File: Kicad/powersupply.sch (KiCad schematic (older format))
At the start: 1 part, among them J601 USB_B

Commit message: Completed PSU design.
Also changed footprint for stacked USB connector to change
shield pins from SHx to Pin 9.
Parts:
- removed J601: USB_B, Connector_USB:USB_B_OST_USB-B1HSxx_Horizontal, symbol Connector:USB_B
- added C601, C602: 100u, Capacitor_THT:CP_Radial_D6.3mm_P2.50mm, symbol Device:CP
- added C603: 22u, Capacitor_THT:CP_Radial_D6.3mm_P2.50mm, symbol Device:CP
- added C604, C608: 100n, Capacitor_SMD:C_0805_2012Metric_Pad1.15x1.40mm_HandSolder, symbol Device:C
- added C605: 47u, Capacitor_THT:CP_Radial_D6.3mm_P2.50mm, symbol Device:CP
- added C606: 1u, Capacitor_THT:CP_Radial_D6.3mm_P2.50mm, symbol Device:CP
- added C607: 4u7, Capacitor_THT:CP_Radial_D6.3mm_P2.50mm, symbol Device:CP
- added D601: LED, LED_THT:LED_D3.0mm, symbol Device:LED
- added F601: 5A Polyfuse, Fuse:Fuse_Littelfuse_395Series, symbol Device:Polyfuse
- added J601: Jack-DC, Connector_BarrelJack:BarrelJack_CUI_PJ-063AH_Horizontal, symbol Connector:Jack-DC
- added J602: Conn_01x04, Connector_PinSocket_2.54mm:PinSocket_1x04_P2.54mm_Vertical, symbol Connector_Generic:Conn_01x04
- added J603: Double-mini-DIN-6, Neotron-Common-Hardware:Double_mini-DIN_6, symbol Neotron-Common-Hardware:Double-mini-DIN-6
- added L601: 22u, Inductor_THT:L_Axial_L23.4mm_D12.7mm_P7.62mm_Vertical_Vishay_IHA-203, symbol Device:L
- added R601, R602, R603, R604, R605, R606: 100k, Resistor_SMD:R_0805_2012Metric_Pad1.15x1.40mm_HandSolder, symbol Device:R
- added R607: 1k, Resistor_SMD:R_0805_2012Metric_Pad1.15x1.40mm_HandSolder, symbol Device:R
- added RN601: 2k7 x 4, Resistor_THT:R_Array_SIP5, symbol Device:R_Network04
- added SW601, SW602: SW_DIP_x01, Connector_PinHeader_2.54mm:PinHeader_1x02_P2.54mm_Vertical, symbol Switch:SW_DIP_x01
- added TP601: TestPoint, TestPoint:TestPoint_THTPad_2.0x2.0mm_Drill1.0mm, symbol Connector:TestPoint
- added U601: K7805-3AR3, Connector_PinSocket_2.54mm:PinSocket_1x12_P2.54mm_Vertical, symbol Neotron-Common-Hardware:K78xx-3AR3
- added U602: AMS1117CD-3.3, Package_TO_SOT_SMD:TO-252-3_TabPin2, symbol Regulator_Linear:AMS1117CD-3.3
- added U603: MAX1615xUK, Package_TO_SOT_SMD:SOT-23-5, symbol Regulator_Linear:MAX1615xUK
- added U604: NUC029FAE, Package_SO:TSSOP-20_4.4x6.5mm_P0.65mm, symbol Neotron-Common-Hardware:NUC029FAE
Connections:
- net labels added: +3.3V, +3V3, +5V, +5VP, DC_ON, GND, I2C_SCL, I2C_SDA, ICE_CLK, ICE_DAT, IRQ, MONITOR_3V3, MONITOR_5V, PS2_CLK0, PS2_CLK1, PS2_DAT0, PS2_DAT1, STATUS_LED, UART0_TX, ~POWER_SW, ~RESET, ~RESET_OUT, ~RESET_SW
- wire segments 0 -> 140
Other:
- note added: "2.51mm (inner, 5.5mm outer diameter) barrel\njack. Centre +ve. 8V to 28V input."
- note added: "28V max input\n30mA max output"
- note added: "36V max input\n3A max output"
- note added: "BSP Debug"
- note added: "Board Management MCU"
- note added: "Dual mini-DIN 6 connectors for PS/2 Keyboard and PS/2 Mouse.\nSignalling is 5V open-collector, with pull-up required.\n\nKeyboard max current is 275 mA so cannot be run from\nstandby regulator."
- note added: "Keyboard"
- note added: "Main Power Regulators"
- note added: "Manual reset switch"
- note added: "Most of our board runs on 3.3V. We expect\nto draw around 100 mA from this 1A linear\nregulator.\n\nMax power wasted: (5V - 3.3V) * 1A = 1.7W\n\nAt 50 °C/W that's 85 °C over ambient at the\njunction - so use a heatsink if you want to\npull over 250 mA. Or replace with a\n3-terminal switching PSU module."
- note added: "Mouse"
- note added: "PS/2 Keyboard and Mouse Interface"
- note added: "Place near U604"
- note added: "Soft power switch"
- note added: "Some of our board (e.g. USB) runs on 5V. We need to\nsupply 2A (4x500mA) to downstream USB devices.\nWe use a big 3A/5V DC-DC to supply this."
- note added: "This MCU controls power/reset.\n\nLines to host are tri-state until host is\npowered to avoid back-powering."
- note added: "This small PSU runs our\nboard management MCU"
- note removed: "The USB Type-B port is used as a 5V input for the system.\nYou could use a 2.51mm (inner, 5.5mm outer diameter) barrel\njack instead."

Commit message: Replaced NUC029 (TSSOP) with KE04 (SOIC).
Also updated the BOM with some part nos.
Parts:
- removed U604: NUC029FAE, Package_SO:TSSOP-20_4.4x6.5mm_P0.65mm, symbol Neotron-Common-Hardware:NUC029FAE
- added R605: 33k, Resistor_SMD:R_0805_2012Metric_Pad1.15x1.40mm_HandSolder, symbol Device:R
- added U604: MKE04P24M48SF0, Package_SO:SOIC-20W_7.5x12.8mm_P1.27mm, symbol Neotron-Common-Hardware:MKE04P24M48SF0
- C601, C602: value 100u -> 100u 50V; DNP (none) -> 0
- C603, C605, C607, D601, J602, L601, R601, R602, R603, RN601, SW601, SW602: DNP (none) -> 0
- C604, C608: DNP (none) -> 0; Digikey (none) -> BC1150CT-ND; MPN (none) -> K104K15X7RF5TL2; Manufacturer (none) -> Vishay
- C606: value 1u -> 1u 50V; DNP (none) -> 0; Digikey (none) -> 493-10944-1-ND; MPN (none) -> UFG1H010MDM1TD; Manufacturer (none) -> Nichicon
- F601: value 5A Polyfuse -> 6A PTC; footprint Fuse:Fuse_Littelfuse_395Series -> Fuse:Fuse_Bourns_MF-RG500; DNP (none) -> 0; Digikey (none) -> MF-R500-2CT-ND; MPN (none) -> MF-R500-2; Manufacturer (none) -> Bourns
- J601: DNP (none) -> 0; Digikey (none) -> CP-063AH-ND; MPN (none) -> PJ-063AH; Manufacturer (none) -> CUI
- J603: MPN (none) -> KMDGX-6S/6S-S4N; Manufacturer (none) -> Kycon
- R604: value 100k -> 1k; DNP (none) -> 0
- R606: renamed from R605; DNP (none) -> 0
- R607: value 1k -> 100k; DNP (none) -> 0
- R608: renamed from R606; DNP (none) -> 0
- TP601: value TestPoint -> Reset; DNP (none) -> 0
- U601: value K7805-3AR3 -> 5V DC-DC Module; DNP (none) -> 0; Digikey (none) -> 2725-K7805-3AR3-ND; MPN (none) -> K7805-3AR3; Manufacturer Mornsun -> Mornsun America, LLC
- U602: value AMS1117CD-3.3 -> 3v3 LDO; DNP (none) -> 0; Digikey (none) -> ZLDO1117K33DICT-ND; MPN (none) -> ZLDO1117K33TC; Manufacturer (none) -> Diodes Incorporated
- U603: value MAX1615xUK -> MAX1615; DNP (none) -> 0; Digikey (none) -> MAX1615EUK+TCT-ND; MPN (none) -> MAX1615; Manufacturer (none) -> Maxim
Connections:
- net labels added: MON_3V3, MON_5V, SWDCLK, SWDIO
- net labels removed: ICE_CLK, ICE_DAT, MONITOR_3V3, MONITOR_5V, ~RESET_OUT
- wire segments 140 -> 144
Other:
- note added: "BMC Debug"
- note added: "Board Management Controller"
- note added: "Manual reset switch:\nTap for reset"
- note added: "Soft power switch:\nTap for On/Shutdown\nHold for Off"
- note added: "The BMC controls power/reset, as well\nas PS/2 devices and performing voltage\nrail monitoring.\n\nLines to host are hi-Z until host is\npowered (i.e. 3.3V looks good) to\navoid back-powering."
- note removed: "BSP Debug"
- note removed: "Board Management MCU"
- note removed: "Manual reset switch"
- note removed: "Soft power switch"
- note removed: "This MCU controls power/reset.\n\nLines to host are tri-state until host is\npowered to avoid back-powering."
- moved on the sheet: C608, R606, R608, SW601, SW602, TP601

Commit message: Make CPU card bigger.
Just big enough to take a TQFP-176 now.
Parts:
- TP601: DNP 0 -> 1
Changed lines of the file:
@@
 $Descr A4 11693 8268
 encoding utf-8
-Sheet 6 9
+Sheet 6 8
 Title "Neotron Common Hardware - Power Supply"
 Date "2020-12-26"
@@
 F 2 "TestPoint:TestPoint_THTPad_2.0x2.0mm_Drill1.0mm" H 7675 4475 50  0001 C CNN
 F 3 "~" H 7675 4475 50  0001 C CNN
-F 4 "0" H 7475 4475 50  0001 C CNN "DNP"
+F 4 "1" H 7475 4475 50  0001 C CNN "DNP"
 	1    7475 4475
 	0    -1   1    0

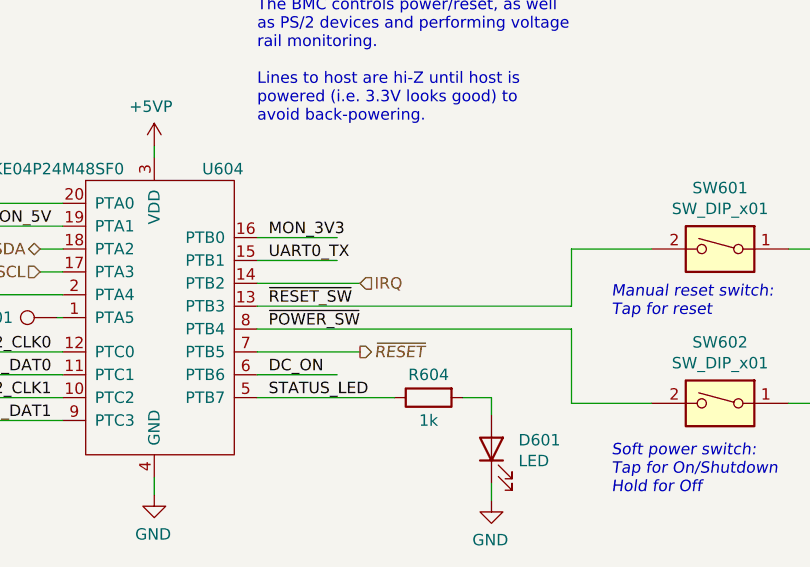
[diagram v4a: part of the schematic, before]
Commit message: Revised CPU connector to be two 2x20.
This gives more room for larger TQFP-176+ CPUs to be fitted that
didn't fit on the PGA-80 design.
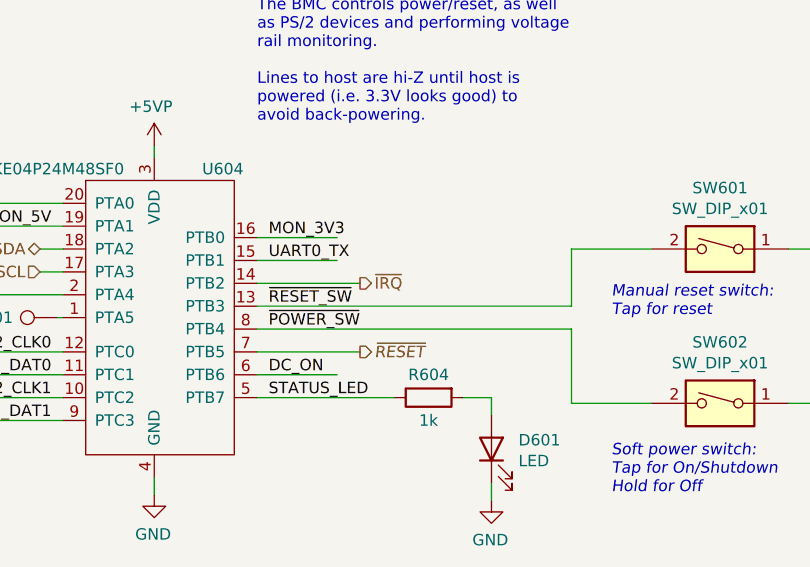
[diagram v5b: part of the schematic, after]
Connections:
- net labels added: ~IRQ
- net labels removed: IRQ
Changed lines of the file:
@@
 Text HLabel 7400 4275 0    50   Input ~ 0
 I2C_SCL
-Text HLabel 8800 4325 2    50   Input ~ 0
-IRQ
+Text HLabel 8800 4325 2    50   Output ~ 0
+~IRQ
 Wire Wire Line
 	7500 4275 7400 4275

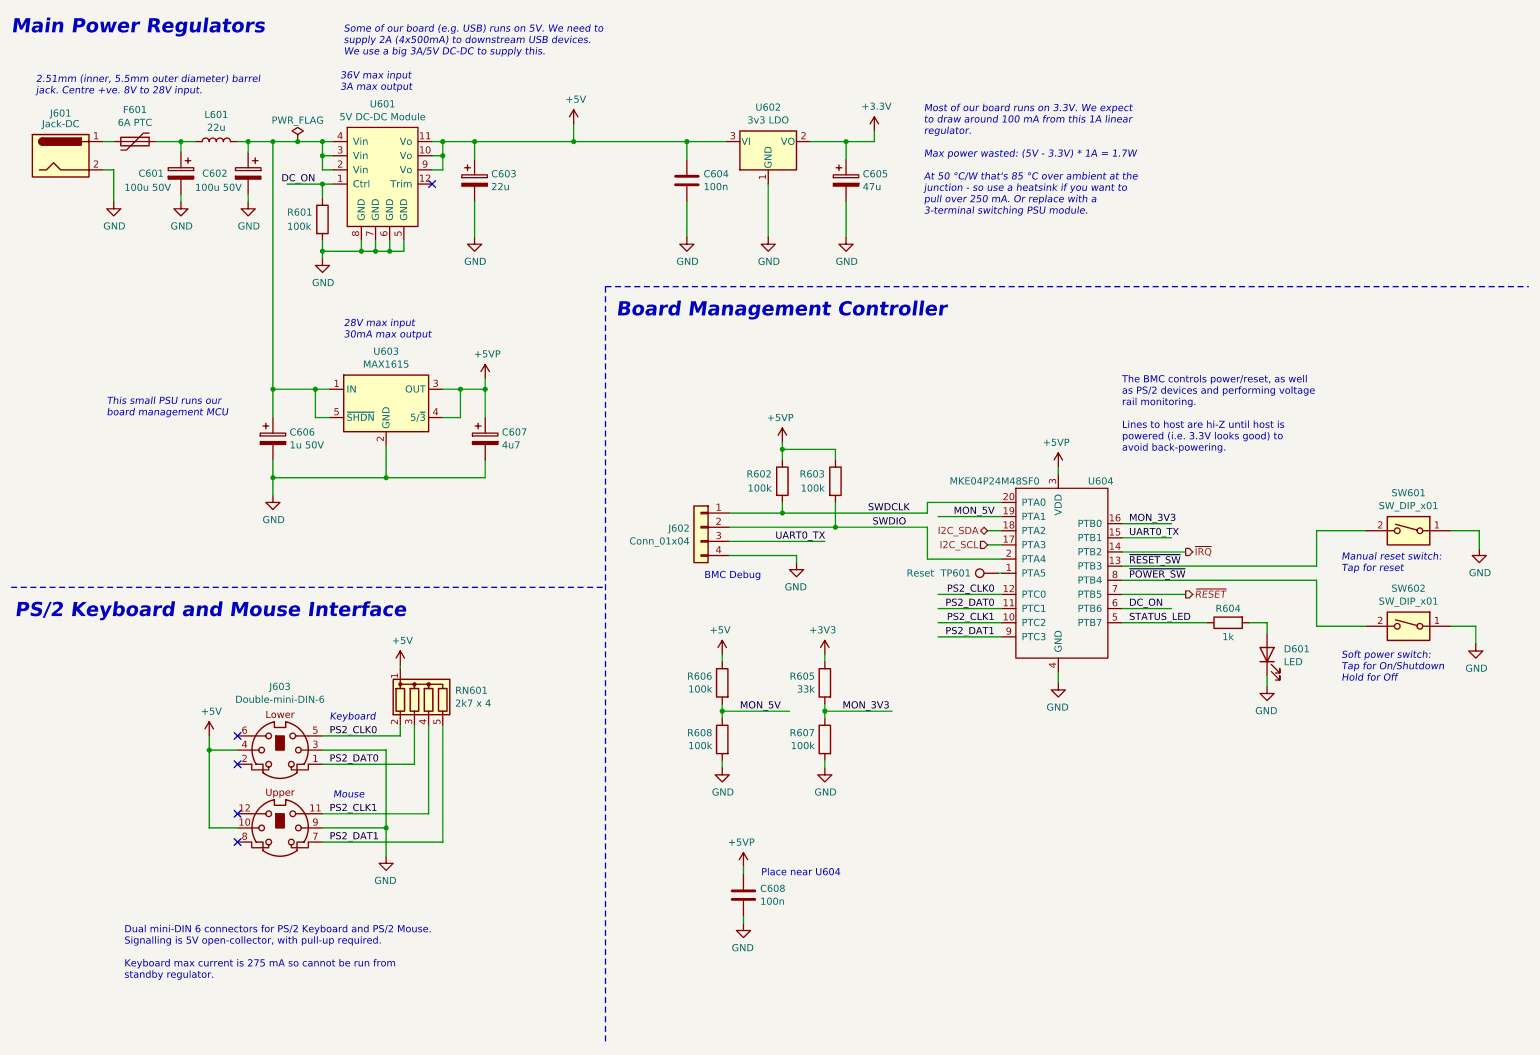
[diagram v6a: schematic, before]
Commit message: Bring in R2R DAC from Neotron-9X schematic.
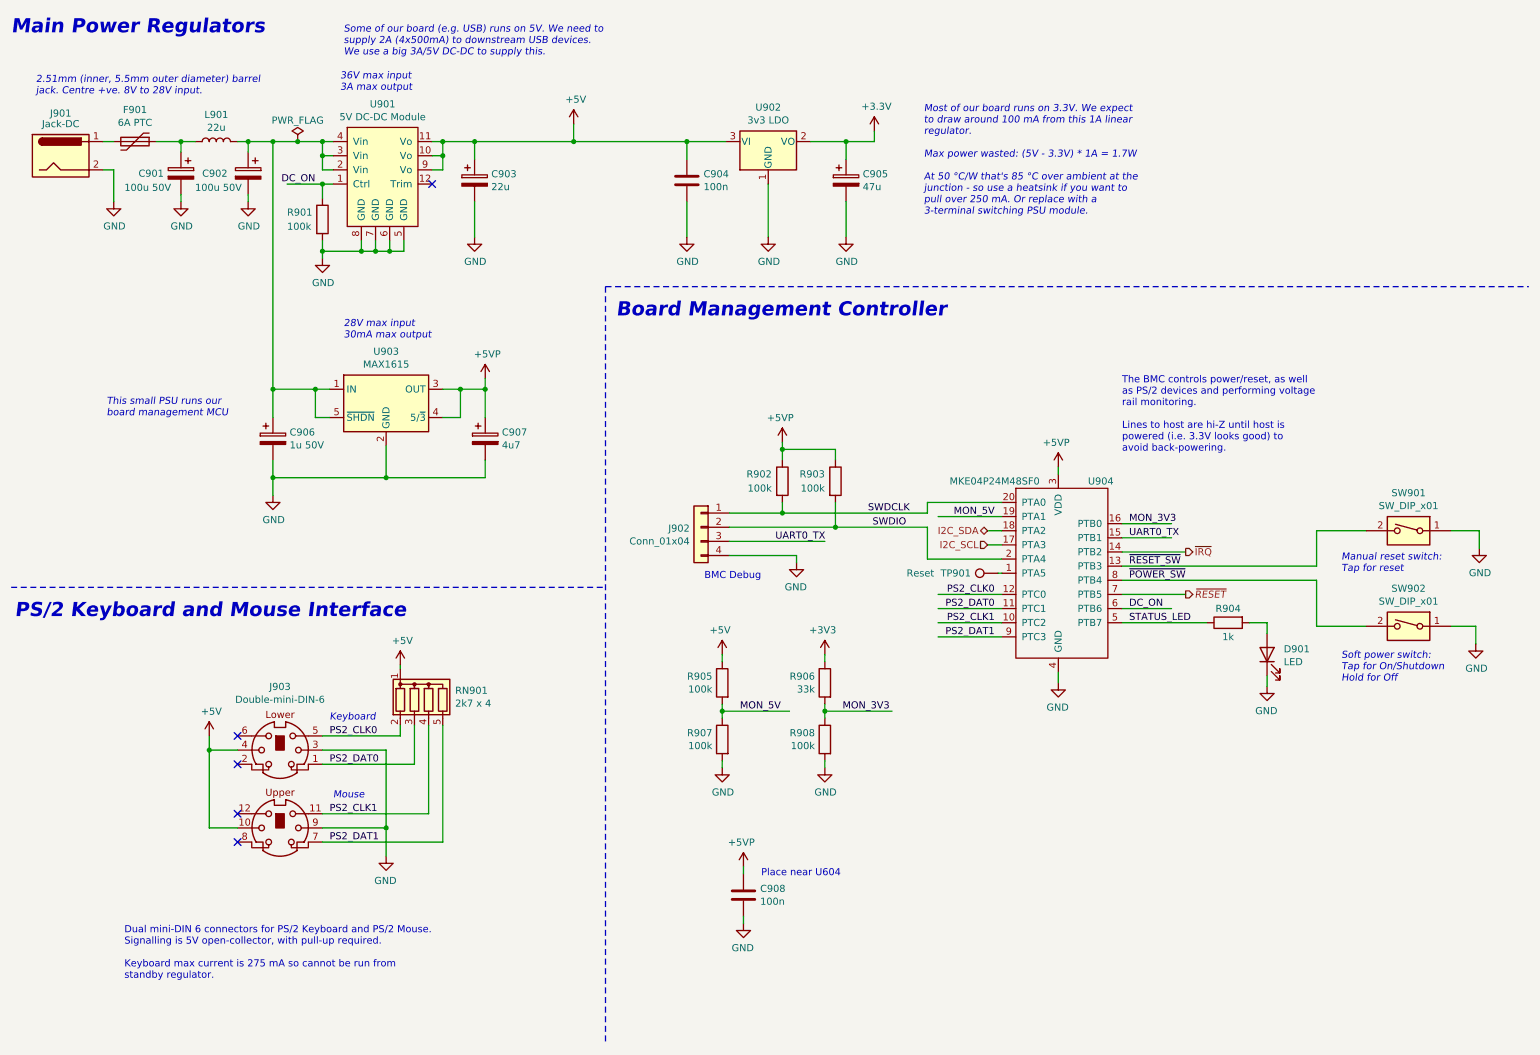
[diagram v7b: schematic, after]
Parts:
- renumbered C601 to C901, C602 to C902, C603 to C903, C604 to C904, C605 to C905, C606 to C906, C607 to C907, C608 to C908, D601 to D901, F601 to F901, J601 to J901, J602 to J902, J603 to J903, L601 to L901, R601 to R901, R602 to R902, R603 to R903, R604 to R904, R606 to R905, R605 to R906, R608 to R907, R607 to R908, RN601 to RN901, SW601 to SW901, SW602 to SW902, TP601 to TP901, U601 to U901, U602 to U902, U603 to U903, U604 to U904

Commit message: Replaced KE04Z with STM32F0.
Had trouble debugging a test KE06Z device. Decided an STM32 would be simpler.
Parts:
- removed J902: Conn_01x04, Connector_PinSocket_2.54mm:PinSocket_1x04_P2.54mm_Vertical, symbol Connector_Generic:Conn_01x04
- removed R903: 100k, Resistor_SMD:R_0805_2012Metric_Pad1.15x1.40mm_HandSolder, symbol Device:R
- removed U904: MKE04P24M48SF0, Package_SO:SOIC-20W_7.5x12.8mm_P1.27mm, symbol Neotron-Common-Hardware:MKE04P24M48SF0
- added C908: 100n, Capacitor_SMD:C_0805_2012Metric_Pad1.15x1.40mm_HandSolder, symbol Device:C
- added JP901: Jumper, Connector_PinHeader_2.54mm:PinHeader_1x02_P2.54mm_Vertical, symbol Device:Jumper_NO_Small
- added JP902, JP903: Jumper, Connector_PinHeader_2.54mm:PinHeader_1x02_P2.54mm_Vertical, symbol Device:Jumper_NC_Small
- added Q901: BC548, Package_TO_SOT_THT:TO-92_HandSolder, symbol Transistor_BJT:BC548
- added R904, R907: 10k, Resistor_SMD:R_0805_2012Metric_Pad1.15x1.40mm_HandSolder, symbol Device:R
- added TP902, TP903: TestPoint, Connector_PinHeader_2.54mm:PinHeader_1x01_P2.54mm_Vertical, symbol Connector:TestPoint
- added U904: STM32F030F4Px, Package_SO:TSSOP-20_4.4x6.5mm_P0.65mm, symbol MCU_ST_STM32F0:STM32F030F4Px
- C905: value 47u -> 1u; footprint Capacitor_THT:CP_Radial_D6.3mm_P2.50mm -> Capacitor_SMD:C_0805_2012Metric_Pad1.15x1.40mm_HandSolder; symbol Device:CP -> Device:C
- F901: value 6A PTC -> 32V 2A PTC; footprint Fuse:Fuse_Bourns_MF-RG500 -> Fuse:Fuse_BelFuse_0ZRE0016FF_L9.9mm_W3.8mm; Digikey MF-R500-2CT-ND -> 507-0ZRS0200FF1E-ND; MPN MF-R500-2 -> 0ZRS0200FF1E; Manufacturer Bourns -> Bel Fuse
- L901: value 22u -> 22uH 6A; footprint Inductor_THT:L_Axial_L23.4mm_D12.7mm_P7.62mm_Vertical_Vishay_IHA-203 -> Inductor_THT:L_Axial_L26.0mm_D11.0mm_P7.62mm_Vertical_Fastron_77A; Digikey (none) -> AIAP-03-220K-ND; MPN (none) -> AIAP-03-220K; Manufacturer (none) -> Abracon
- R901: value 100k -> 2k
- R902, R905, R908: value 100k -> 10k
- R906: value 33k -> 10k
- R909: renamed from R907; value 100k -> 10k
- SW901, SW902: DNP 0 -> 1
- TP901: value Reset -> TestPoint; footprint TestPoint:TestPoint_THTPad_2.0x2.0mm_Drill1.0mm -> Connector_PinHeader_2.54mm:PinHeader_1x01_P2.54mm_Vertical
- U902: value 3v3 LDO -> TLV1117 3.3V 1A; footprint Package_TO_SOT_SMD:TO-252-3_TabPin2 -> Package_TO_SOT_SMD:SOT-223-3_TabPin2; Digikey ZLDO1117K33DICT-ND -> 296-28778-1-ND; MPN ZLDO1117K33TC -> TLV1117LV33DCYR; Manufacturer Diodes Incorporated -> Texas Instruments
- U903: MPN MAX1615 -> MAX1615EUK+T
- renumbered C908 to C909, J903 to J902, R904 to R903
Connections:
- net labels added: +3.3VP, BOOT0, SCL_U1TX, SDA_U1RX, USART1_TX, ~BMC_RST, ~BUTTON_PWR, ~BUTTON_RST, ~PSU_EN, ~STATUS_LED
- net labels removed: +5VP, STATUS_LED, SWDCLK, SWDIO, UART0_TX, ~POWER_SW, ~RESET_SW
- wire segments 144 -> 166
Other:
- note added: "1.65V\nnominal"
- note added: "2.51mm (inner, 5.5mm outer diameter) barrel\njack. Centre +ve. 12V nominal."
- note added: "BOOT0 = 0 => Run Program\nBOOT0 = 1 => Bootloader"
- note added: "Some of our board (e.g. USB) runs on 5V. We also need\nto supply 2A (4x500mA) to downstream USB devices.\nWe use a big 3A/5V DC-DC to supply this."
- note added: "UART Programming:\n* Fit jumper to JP901\n* Remove jumper from J902 and J903\n* Connect J902 Pin 1 to UART RX\n* Connect J903 Pin 1 to UART TX\n* Connect DC power"
- note removed: "2.51mm (inner, 5.5mm outer diameter) barrel\njack. Centre +ve. 8V to 28V input."
- note removed: "BMC Debug"
- note removed: "Some of our board (e.g. USB) runs on 5V. We need to\nsupply 2A (4x500mA) to downstream USB devices.\nWe use a big 3A/5V DC-DC to supply this."
- moved on the sheet: C909, D901, R903, R905, R906, R908, R909, SW901, SW902
